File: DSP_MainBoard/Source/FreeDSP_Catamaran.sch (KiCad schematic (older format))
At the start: 252 parts, among them IC1 ADAU1701, IC2 24AA256, IC3 24AA256, J1 Conn_01x02, J10 Conn_01x02, J11 HeaderPin_01x03, J12 B3B-XH, J13 B3B-XH, J14 B3B-XH, J15 Molex 1718563002, J16 Conn_01x03, J2 Conn_RCA, J3 Conn_02x5_Odd_Even, J4 Conn_RCA, J5 Conn_RCA, J6 Conn_RCA, J7 Conn_01x07_Male, J8 Conn_RCA, J9 Conn_Power_2.1mm, P1 MIL-10P_Angle, Q1 2SC3326, Q10 AO3401A, Q11 AO3400A, Q12 AO3401A, Q13 AO3400A, Q2 AO3400A, Q3 2SC3326, Q5 2SC3326, Q6 AO3401A, Q7 2SC3326, Q8 KTA1040D-Y-RTF/P, Q9 AO3400A, SW1 2MS1T1B4M7QES, SW2 2MS1T1B4M7QES, U1 OPA1611, U2 SN74LV541APWR, U3 OPA1611, U4 OPA1652, U5 OPA1611, U6 AZ1117-ADJ, U7 AZ1117-ADJ, U8 OPA1611, U9 OPA1632DR, X2 3N12288G33YC

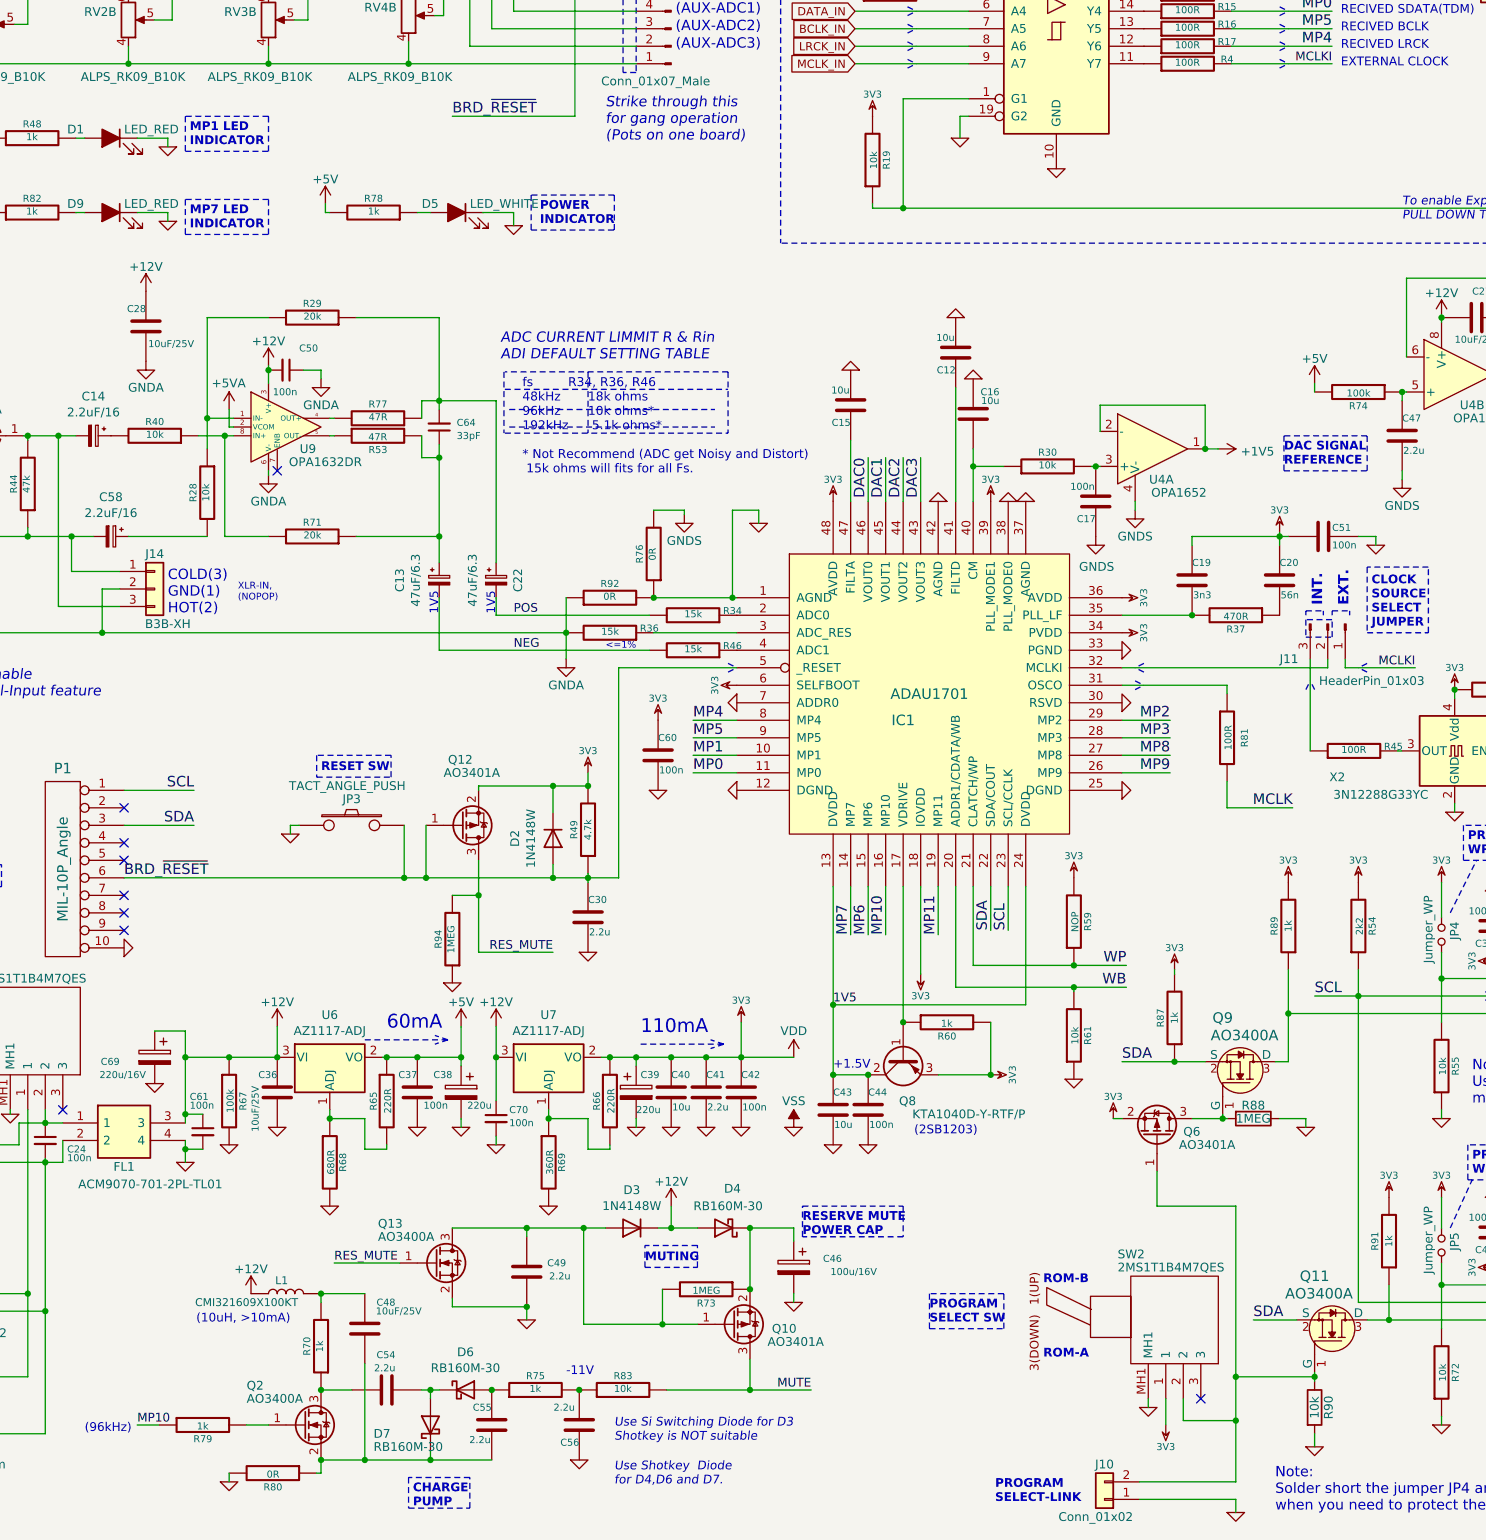
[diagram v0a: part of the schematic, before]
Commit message: 1v2 add auto-reboot feature on PGM-SW transnsition
The reset switch was removed due to the automatic DSP reboot feature on the transition of the A/B program change.
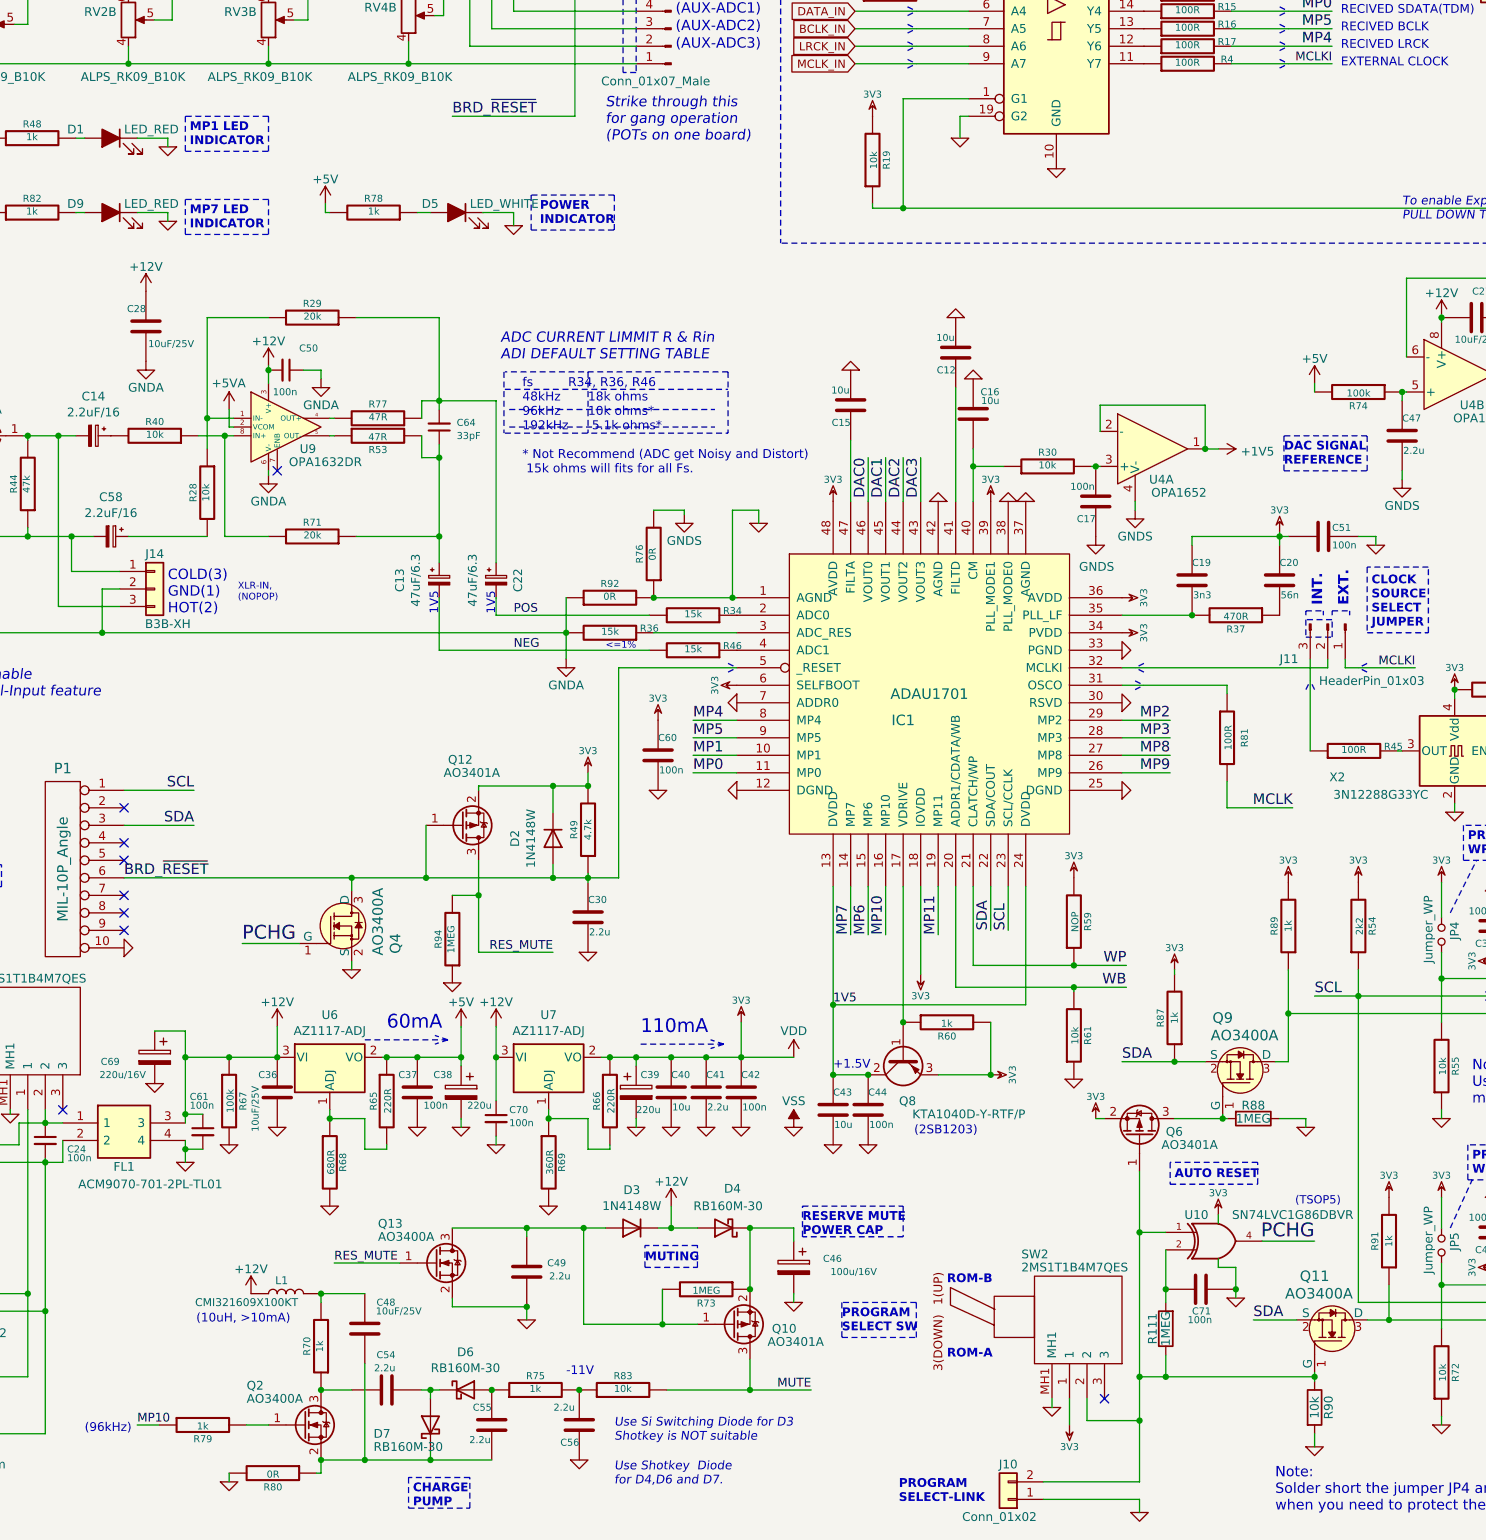
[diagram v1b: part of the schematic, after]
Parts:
- removed JP3: TACT_ANGLE_PUSH, Button_Switch_THT:SW_Tactile_SPST_Angled_PTS645Vx83-2LFS, symbol fdsp_mechanical:SW_PUSH
- added C71: 100n, Capacitors_SMD:C_0805_HandSoldering, symbol FreeDSP_SMD_AB_plus-rescue:C-RESCUE-FreeDSP_SMD-FreeDSP_SMD-rescue-FreeDSP_SMD-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
- added Q4: AO3400A, digikey-footprints:SOT-23-3, symbol USBi_Programmer-rescue:2N7002-dk_Transistors-FETs-MOSFETs-Single
- added R111: 1MEG, Resistors_SMD:R_0805_HandSoldering, symbol Device:R
- added U10: SN74LVC1G86DBVR, Package_TO_SOT_SMD:TSOT-23-5, symbol 74xGxx:74AHC1G86
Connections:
- net 3V3: now also U10.5 (VCC)
- net BRD_~RESET: now also Q4.3 (D)
- net GND: now also C71.1, Q4.2 (S), U10.3 (GND)
- net at J10.2 (Pin_2), Q11.1 (G), Q6.1 (G)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: now also R111.1, U10.1
- new net: C71.2, R111.2, U10.2
- new net PCHG: Q4.1 (G), U10.4
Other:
- note added: "(TSOP5)"
- note added: "AUTO RESET"
- note added: "Strike through this\nfor gang operation\n(POTs on one board)"
- note removed: "RESET SW"
- note removed: "Strike through this\nfor gang operation\n(Pots on one board)"
- moved on the sheet: J10, Q6, SW2
